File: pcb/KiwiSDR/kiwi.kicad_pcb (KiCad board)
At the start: 6 copper layers, 117 x 55 mm, 177 parts, among them J1 TB_2, J2 DNL BNC, J3 SMA, J4 DNL U.FL, J5 DNL U.FL, U1 Artix-7 A35, U101 SE4150L, U104 LP5907 3.3V 250mA, U301 EEPROM 32Kx8, U401 LTC2248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

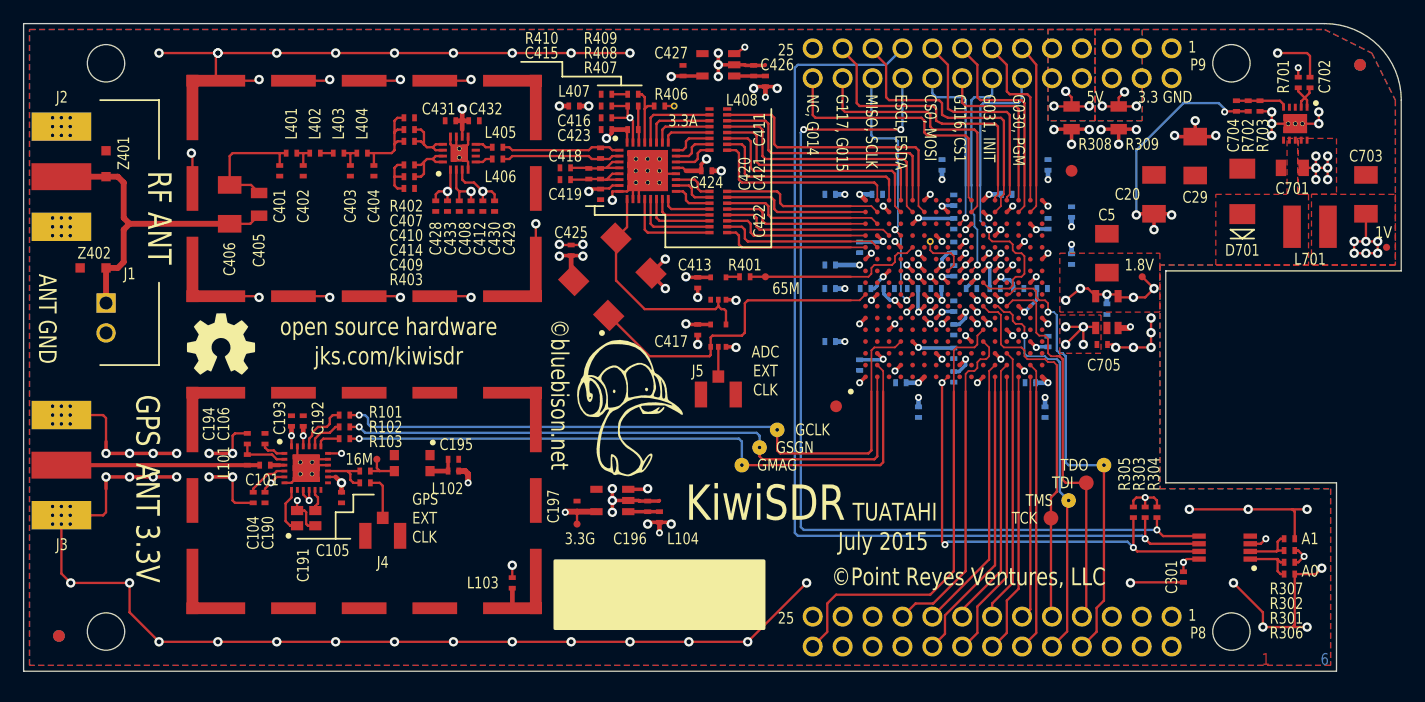
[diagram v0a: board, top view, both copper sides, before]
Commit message: v0.5 PCB with 5V DC input
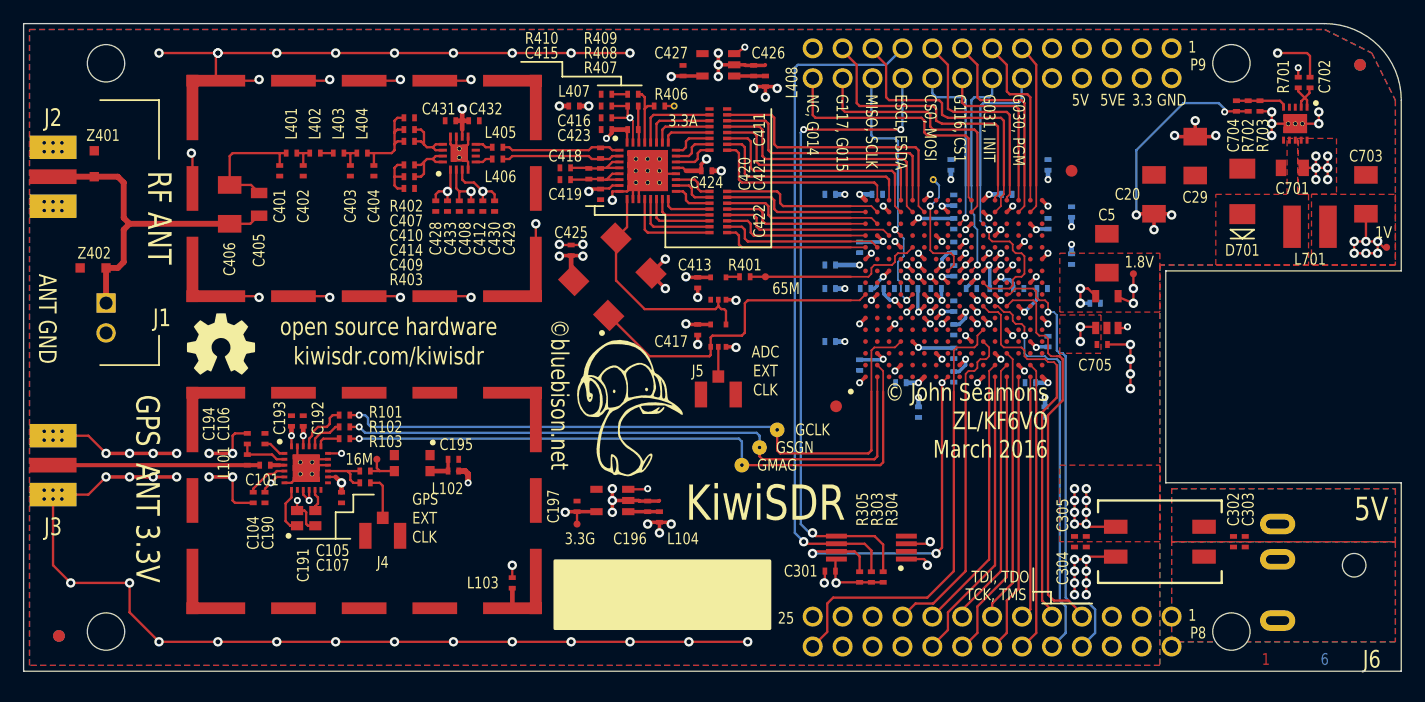
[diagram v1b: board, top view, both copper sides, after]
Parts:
- removed R301, R302: 5K6, kiwi-SM0402
- removed R306, R307: 0R, kiwi-SM0402
- removed R308: 0R, kiwi-SM0805
- removed R309: DNL, kiwi-SM0805
- removed TP302, TP303: TEST_POINT, kiwi-TP_1250
- removed TP304, TP305: TEST_POINT, kiwi-TP_VIA_1250
- added C302: 470n, kiwi-SM0402, F.Cu at (178.8, 116.5)
- added C303: 10n, kiwi-SM0402, F.Cu at (179.8, 116.5)
- added C304: 470n, kiwi-SM0402, F.Cu at (165.2, 116.5)
- added C305: 10n, kiwi-SM0402, F.Cu at (166.2, 116.5)
- added J6: POWER JACK 2.1MM, kiwi-JACK_2_1MM_TH, F.Cu at (193.0, 118.5)
- added T301: CMC 500uH 1A, kiwi-CMC, F.Cu at (172.5, 116.5)
- J2: value DNL BNC -> SMA; footprint kiwi-BNC_SMA_EM -> kiwi-SMA_OPL_EM
- J3: footprint kiwi-SMA_EM -> kiwi-SMA_OPL_EM
- TP301: moved to F.Cu
- ZB1: value BEAGLEBONE_BLACK -> HEADER 13x2
- moved C301 30.0 mm to (144.5, 119.0), turned to 0 degrees
- moved U301 30.0 mm to (148.0, 117.0)
- moved R303 23.9 mm to (148.0, 119.5), turned to 90 degrees
- moved R304 23.9 mm to (149.0, 119.5), turned to 90 degrees
- moved R305 23.9 mm to (147.0, 119.5), turned to 90 degrees
- moved TP301 5.26 mm to (153.2, 85.8)
- moved J3 4.75 mm to (76.0, 110.0)
- moved C706 1.12 mm to (167.0, 96.2), turned to 0 degrees
- moved Z401 1.00 mm to (82.0, 84.4)
- moved TP702 0.79 mm to (170.2, 93.8)
- moved C18 0.75 mm to (154.8, 84.5)
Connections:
- U301 pad 1: /BeagleBone/EJ1 -> GND
- U301 pad 2: /BeagleBone/EJ2 -> GND
- ZB1 pad 907: 5INT -> 5V
- ZB1 pad 908: 5INT -> 5V
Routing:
- net GND: track 325.8 -> 296.6 mm
- net /BeagleBone/ESCL: track 85.8 -> 58.2 mm
- net /BeagleBone/ESDA: track 81.7 -> 56.3 mm
- net 5V: track 31.5 -> 19.0 mm, vias 26 -> 18
- net EWP: track 39.1 -> 31.5 mm
- net /BeagleBone/DONE: track 4.41 -> 10.2 mm, vias 0 -> 1
- net 5EXT: track 4.37 -> 9.60 mm, vias 3 -> 8
- net /BeagleBone/EJ1: track 4.72 -> 0.00 mm
- net 5INT: track 4.52 -> 0.00 mm, vias 3 -> 0
- net /BeagleBone/EJ2: track 4.31 -> 0.00 mm
- net 1.8: track 19.8 -> 17.0 mm, vias 10 -> 9
- net 3.3: track 66.9 -> 65.3 mm, vias 42 -> 40
- net /BeagleBone/TDO: track 38.6 -> 37.1 mm
- net 1.0: track 46.4 -> 47.3 mm
- net /GPS/GPS: track 17.9 -> 18.6 mm
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- added copper zone on B.Cu, net /BeagleBone/5V_NEG
- added copper zone on F.Cu, net /BeagleBone/5V_NEG
- added copper zone on B.Cu, net /BeagleBone/5V_POS
- added copper zone on F.Cu, net /BeagleBone/5V_POS
- added copper zone on G2, net 5EXT
- removed copper zone on B.Cu, net 5EXT
- removed copper zone on B.Cu, net 5INT
- removed copper zone on F.Cu, net 5INT
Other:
- outline, holes or cut-outs redrawn
- net class 1.8: clearance 0.1 -> 0.15
- net class 10/10: clearance 0.125 -> 0.15
- net class 5V: clearance 0.1 -> 0.15
- net class 5V_IN added: clearance 0.15, trace_width 1, via_dia 0.8, via_drill 0.4
- net class 6/6: clearance 0.075 -> 0.15
- net class 8/8: clearance 0.1 -> 0.15
- net class Default: clearance 0.1 -> 0.15
- net class FPGA: clearance 0.065 -> 0.15
- rule trace_clearance: 0.1 -> 0.15
- board text added: "5VE"
- board text added: "KiwiSDR prototype v0.5 22-Feb-2016"
- board text added: "TCK, TMS"
- board text added: "TDI, TDO"
- board text added: "kiwisdr.com/kiwisdr"
- board text added: "© John Seamons ZL/KF6VO March 2016"
- board text removed: "A0"
- board text removed: "A1"
- board text removed: "DO NOT LOAD RED COMPONENTS"
- board text removed: "July 2015"
- board text removed: "KiwiSDR prototype v0.3 15-July-2015"
- board text removed: "TCK"
- board text removed: "TDI"
- board text removed: "TDO"
- board text removed: "TMS"
- board text removed: "TUATAHI"
- board text removed: "jks.com/kiwisdr"
- board text removed: "©Point Reyes Ventures, LLC"
